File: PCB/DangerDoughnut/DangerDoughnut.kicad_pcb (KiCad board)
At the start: 4 copper layers, 50 x 37 mm, 113 parts, among them J1 Conn_01x02_Pin, J2 Conn_01x02_Pin, J3 Conn_01x02_Pin, J4 Conn_01x04_Pin, J6 USB_C_Receptacle_USB2.0_16P, SW1 SW_Push, SW2 SW_Push, U1 MMC5983MA, U10 ESP32-S3, U2 H3LIS331DLTR, U3 H3LIS331DLTR, U4 W25X20CLZP, U6 L5973D, U7 MIC5219-3.3YM5, U8 ESP8285H16, U9 SX1280IMLTRT, Y1 40MHz, Y2 52MHz, Y3 26MHz

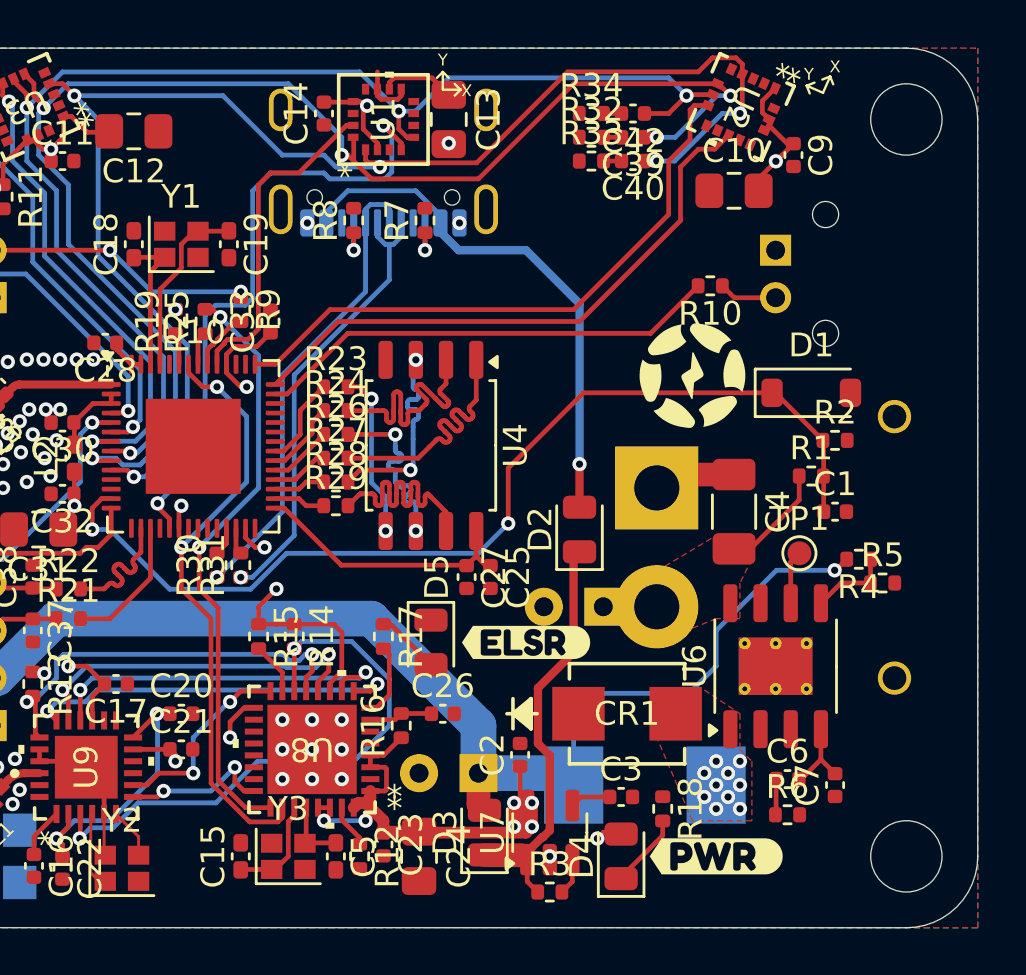
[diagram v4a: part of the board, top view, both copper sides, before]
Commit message: Added silkscreen
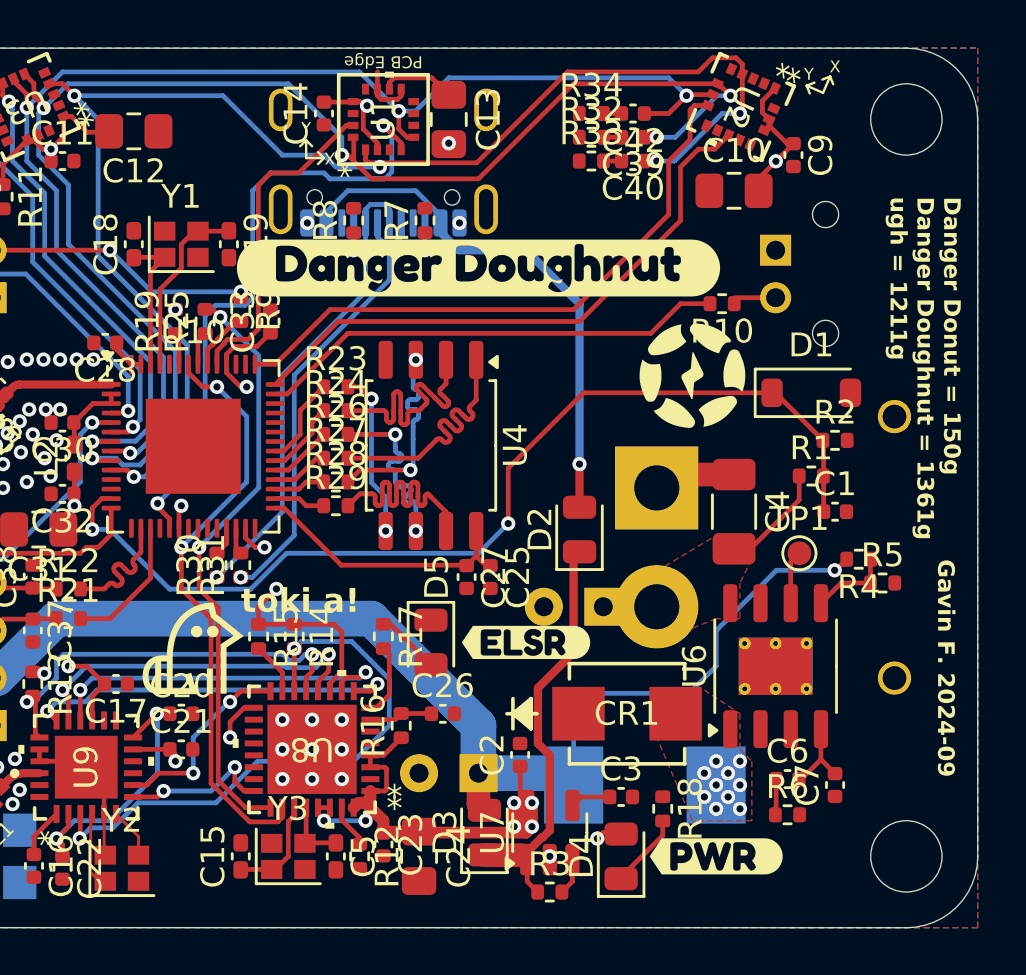
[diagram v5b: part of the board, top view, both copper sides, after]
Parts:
- added kibuzzard-66F236AA: G***, kibuzzard-66F236AA, F.Cu at (104.0, 45.2)
- moved R10 0.90 mm to (114.2, 46.8)
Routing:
- net Net-(J2-Pin_2): track 2.45 -> 1.74 mm
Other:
- board text added: "<--"
- board text added: "<-- Radio waves go here"
- board text added: "Cook Time: 10 minutes Total Time: 2 hours, 30 minutes Yield: 12 donuts and 12 holes Ingredients 1 cup whole milk, warmed to about 110°F 2 and 1/4 teaspoons instant or active dry yeast 1/3 cup granulated sugar, divided 2 large eggs 6 Tablespoons unsalted butter 1/2 teaspoon salt 4 cups all-purpose flour 2 cups confectioners' sugar 1/3 cup heavy cream 1/2 teaspoon pure vanilla extract 1. Prepare th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"
- board text added: "Danger Donut = 150g Danger Doughnut = 1361g ugh = 1211g"
- board text added: "Ferrous metal under the compass! Surely this won't be a problem"
- board text added: "Gavin F. 2024-09"
- board text added: "TODO: layout test points/headers run traces silk screen flip LED wiring move ESC resistors"
- board text added: "toki a!"
- board text removed: "TODO: layout sensors layout esp32 layout test points/headers run traces silk screen flip LED wiring"

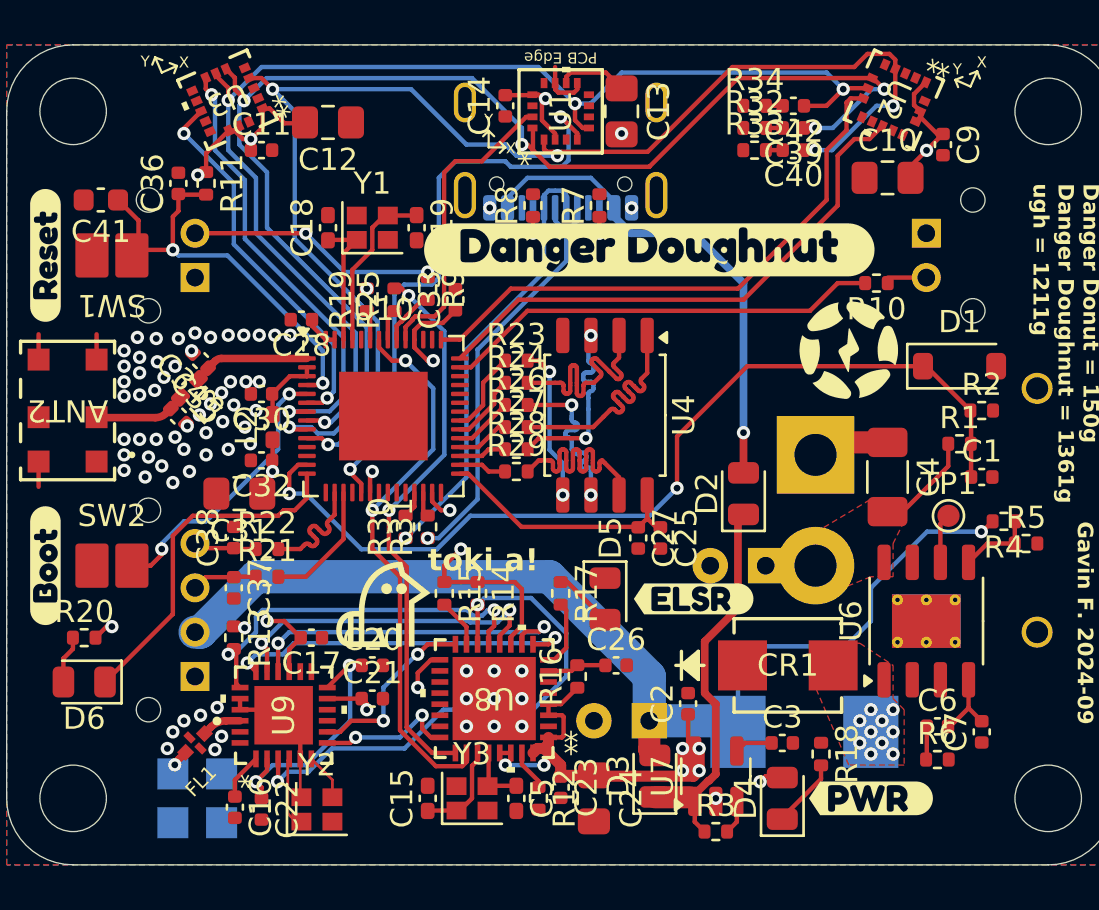
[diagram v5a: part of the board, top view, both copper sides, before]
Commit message: main layout complete needs headers and testpoints
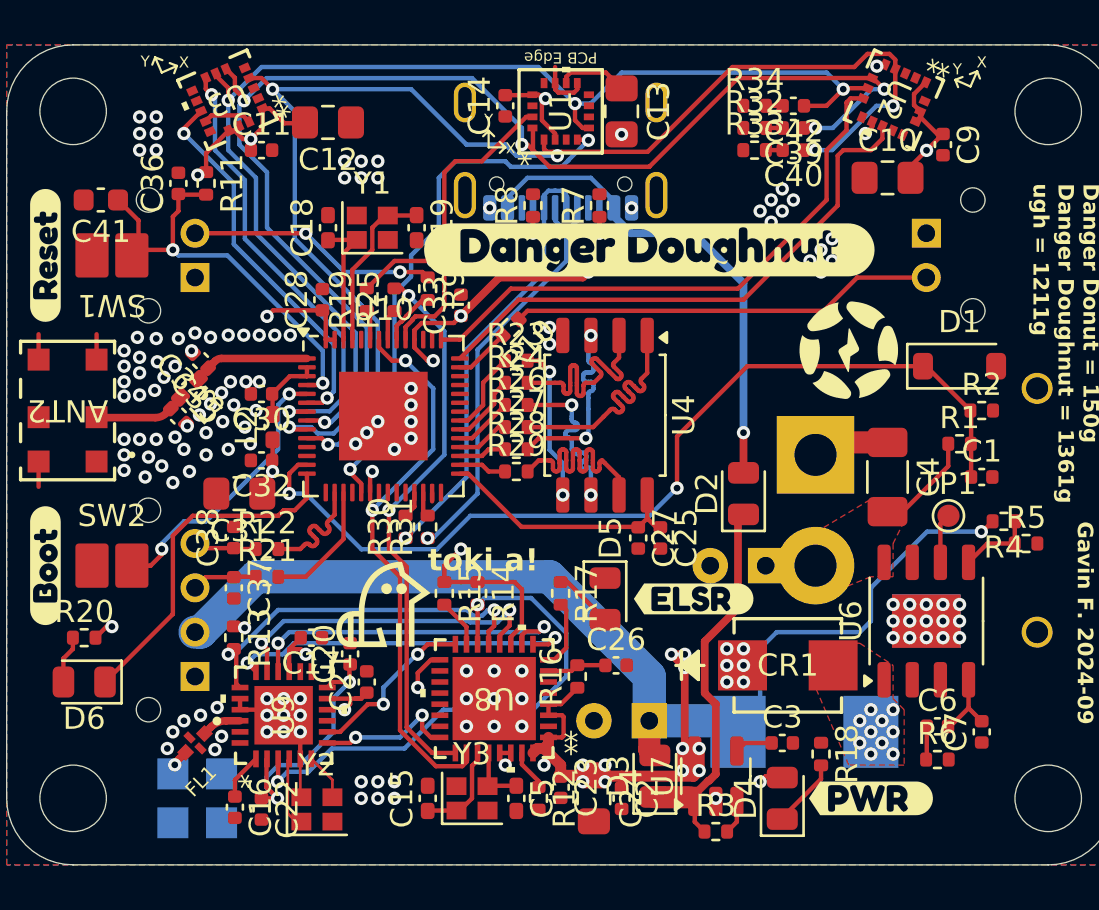
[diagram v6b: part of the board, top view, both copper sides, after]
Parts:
- moved R10 16.6 mm to (97.8, 48.8), turned to -135 degrees
- moved C2 5.22 mm to (102.8, 70.0), turned to -90 degrees
- moved C28 1.31 mm to (89.2, 47.5), turned to 90 degrees
- moved C20 1.13 mm to (90.5, 63.5), turned to 90 degrees
- moved C21 0.79 mm to (91.2, 64.8), turned to 90 degrees
- moved C33 0.35 mm to (95.5, 47.8)
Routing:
- net +3.3V: track 70.3 -> 88.5 mm, vias 20 -> 30
- net Net-(J2-Pin_2): track 1.74 -> 19.2 mm
- net ESC_R: track 19.9 -> 2.54 mm
- net GND: track 16.4 -> 20.4 mm, vias 70 -> 142
- net Mag_CS: track 26.6 -> 24.2 mm
- net unconnected-(U10-GPIO21-Pad27): track 1.37 -> 0.40 mm, vias 1 -> 0
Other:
- board text added: "TODO: layout test points/headers"
- board text removed: "TODO: layout test points/headers run traces silk screen flip LED wiring move ESC resistors"

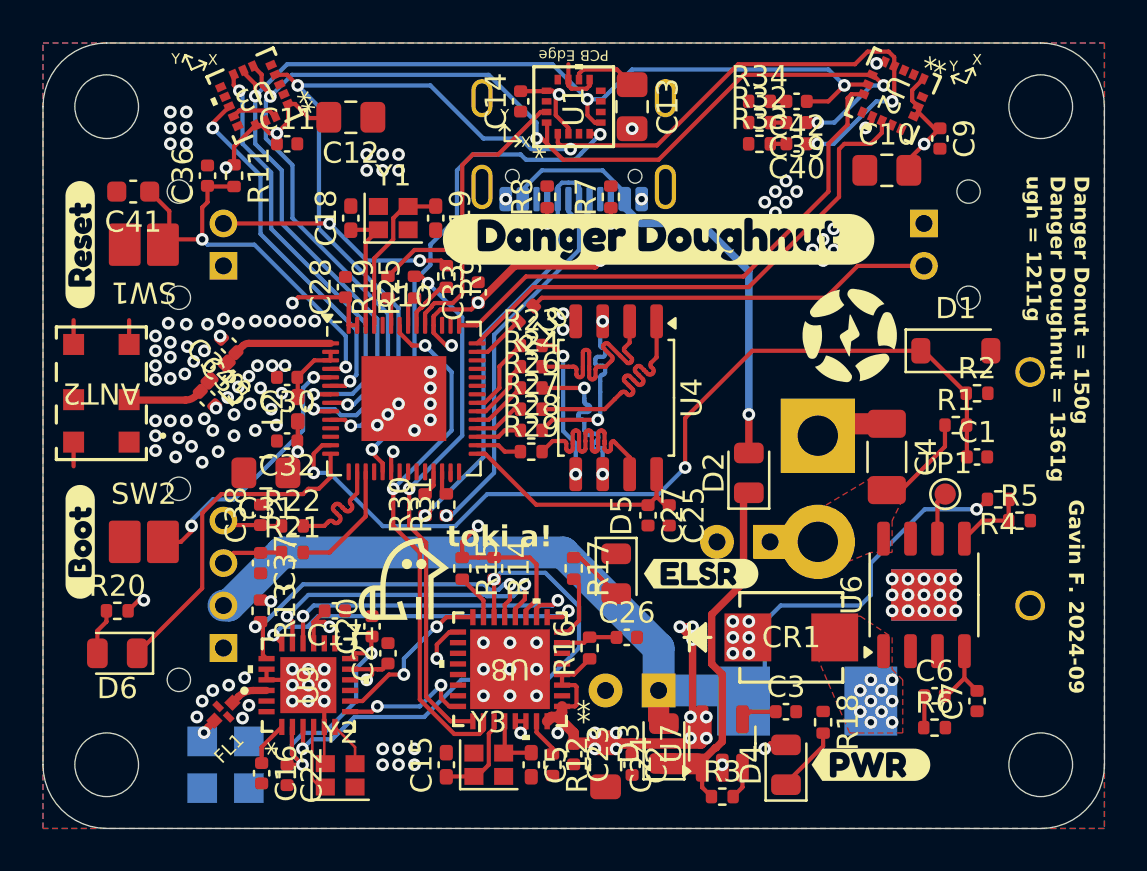
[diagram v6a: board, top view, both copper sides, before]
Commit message: esp32 pins checked
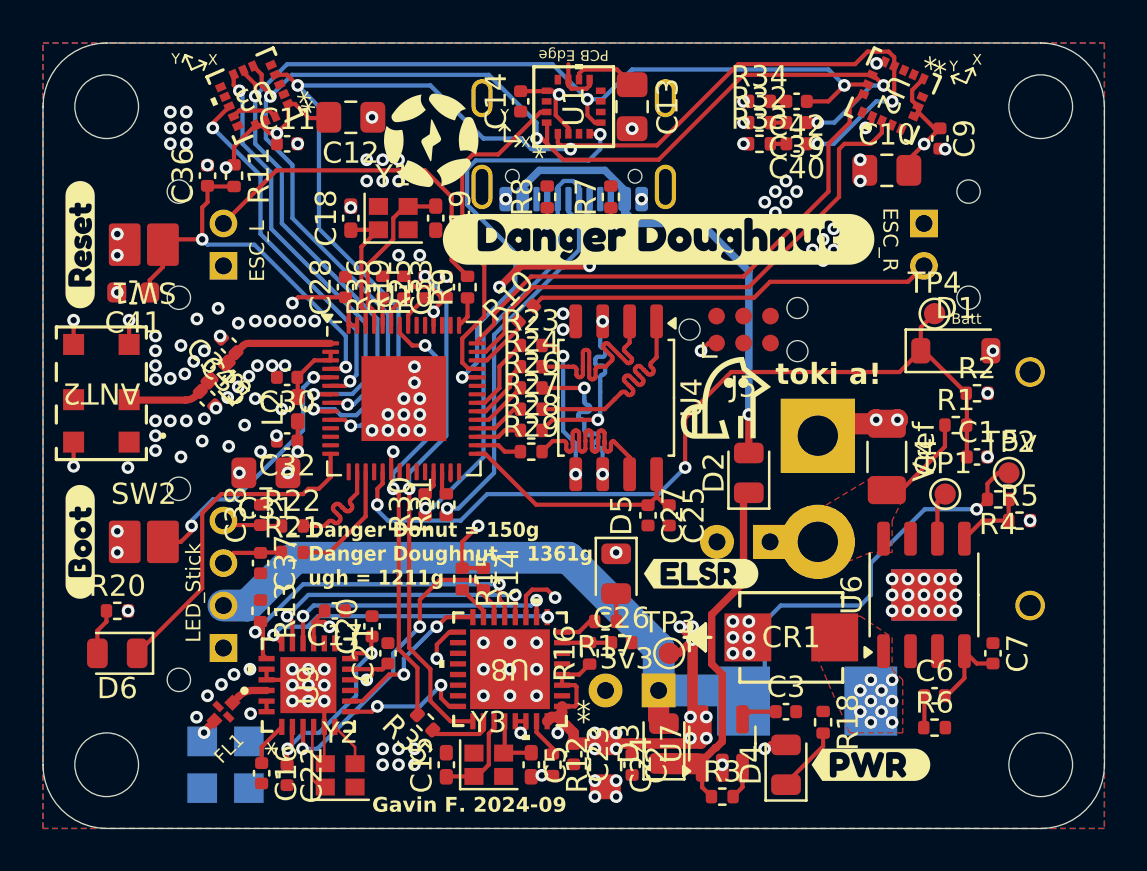
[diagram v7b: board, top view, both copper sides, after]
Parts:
- added J5: TC2030-NL, Connector:Tag-Connect_TC2030-IDC-NL_2x03_P1.27mm_Vertical, F.Cu at (108.0, 49.5)
- added R35: 510, Resistor_SMD:R_0402_1005Metric, F.Cu at (93.0, 68.0)
- added R36: 10K, Resistor_SMD:R_0402_1005Metric, F.Cu at (91.0, 47.5)
- added TP2: 5v, TestPoint:TestPoint_Pad_D1.0mm, F.Cu at (120.5, 56.2)
- added TP3: 3v3, TestPoint:TestPoint_Pad_D1.0mm, F.Cu at (104.5, 64.8)
- added TP4: Batt, TestPoint:TestPoint_Pad_D1.0mm, F.Cu at (117.0, 48.8)
- R10, R9: value 100 -> 33
- moved C41 4.75 mm to (79.2, 47.8)
- moved R17 2.92 mm to (101.5, 63.2), turned to 180 degrees
- moved C7 2.37 mm to (119.8, 64.8), turned to -90 degrees
- moved C33 1.52 mm to (94.0, 47.5)
- moved R9 1.12 mm to (95.0, 47.5), turned to 90 degrees
- moved R19 0.75 mm to (92.0, 47.5)
- moved R14 0.71 mm to (95.8, 61.2)
- moved R15 0.50 mm to (94.8, 61.2)
- moved R25 0.50 mm to (93.0, 47.5)
- moved C26 0.35 mm to (102.2, 64.2)
- moved R16 0.25 mm to (100.8, 64.8)
- turned R10 to 45 degrees
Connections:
- J2 pad 2: Net-(J2-Pin_2) -> ESC_R
- J3 pad 2: Net-(J3-Pin_2) -> ESC_L
- R10 pad 1: Net-(J2-Pin_2) -> Net-(U10-GPIO35)
- R9 pad 1: Net-(J3-Pin_2) -> Net-(U10-GPIO38)
- U10 pad 13: BATT -> unconnected-(U10-GPIO8-Pad13)
- U10 pad 19: Mag_CS -> BATT
- U10 pad 38: unconnected-(U10-GPIO33-Pad38) -> Mag_CS
- U10 pad 39: unconnected-(U10-GPIO34-Pad39) -> MAG_INT
- U10 pad 40: unconnected-(U10-GPIO35-Pad40) -> Net-(U10-GPIO35)
- U10 pad 41: ESC_R -> ACCEL1_INT
- U10 pad 42: ACCEL1_INT -> Accel1_CS
- U10 pad 43: Accel1_CS -> Net-(U10-GPIO38)
- U10 pad 47: MAG_INT -> unconnected-(U10-MTDI-Pad47)
- U10 pad 48: ESC_L -> unconnected-(U10-MTMS-Pad48)
- U10 pad 52: unconnected-(U10-GPIO46-Pad52) -> Net-(U10-GPIO46)
- U8 pad 26: ELSR_TX -> Net-(U8-U0TXD)
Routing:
- net Net-(J2-Pin_2): track 19.2 -> 0.00 mm
- net ESC_R: track 2.54 -> 19.2 mm
- net ESC_L: track 2.53 -> 16.4 mm
- net Net-(J3-Pin_2): track 11.3 -> 0.00 mm, vias 2 -> 0
- net N_RST: track 24.6 -> 15.6 mm
- net +3.3V: track 88.5 -> 82.3 mm, vias 30 -> 32
- net ELSR_TX: track 24.8 -> 20.7 mm
- net Mag_CS: track 24.2 -> 20.4 mm
- net Net-(U8-U0TXD): track 0.00 -> 2.96 mm
- net Net-(U10-GPIO35): track 0.00 -> 2.91 mm
- net MAG_INT: track 13.8 -> 16.0 mm
- net SX_SCK: track 16.1 -> 13.9 mm
- net GND: track 20.4 -> 22.4 mm, vias 142 -> 168
- net BATT: track 42.3 -> 40.4 mm
- net /DCC_FB: track 12.2 -> 10.4 mm
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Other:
- board text added: "ESC_L"
- board text added: "ESC_R"
- board text added: "LED_Stick"

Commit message: test points done
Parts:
- removed J5: TC2030-NL, Connector:Tag-Connect_TC2030-IDC-NL_2x03_P1.27mm_Vertical
- added J10: Conn_01x01_Pin, Connector_Wire:SolderWirePad_1x01_SMD_1x2mm, F.Cu at (123.2, 53.2)
- added J11: Conn_01x01_Pin, Connector_Wire:SolderWirePad_1x01_SMD_1x2mm, F.Cu at (123.2, 60.8)
- added J12: Conn_01x01_Pin, Connector_Wire:SolderWirePad_1x01_SMD_1x2mm, F.Cu at (123.2, 65.8)
- added J13: Conn_01x01_Pin, Connector_Wire:SolderWirePad_1x01_SMD_1x2mm, F.Cu at (123.2, 45.2)
- added J14: Conn_01x01_Pin, Connector_Wire:SolderWirePad_1x01_SMD_1x2mm, F.Cu at (123.2, 57.8)
- added J15: Conn_01x01_Pin, Connector_Wire:SolderWirePad_1x01_SMD_1x2mm, F.Cu at (123.2, 49.8)
- added J16: Conn_01x01_Pin, Connector_Wire:SolderWirePad_1x01_SMD_1x2mm, F.Cu at (123.2, 43.8)
- added J17: Conn_01x01_Pin, Connector_Wire:SolderWirePad_1x01_SMD_1x2mm, F.Cu at (123.2, 48.2)
- added J19: Conn_01x01_Pin, Connector_Wire:SolderWirePad_1x01_SMD_1x2mm, F.Cu at (123.2, 46.8)
- added J20: Conn_01x01_Pin, Connector_Wire:SolderWirePad_1x01_SMD_1x2mm, F.Cu at (123.2, 64.2)
- added J7: Conn_01x01_Pin, Connector_Wire:SolderWirePad_1x01_SMD_1x2mm, F.Cu at (123.2, 56.2)
- added J8: Conn_01x01_Pin, Connector_Wire:SolderWirePad_1x01_SMD_1x2mm, F.Cu at (123.2, 54.8)
- added J9: Conn_01x01_Pin, Connector_Wire:SolderWirePad_1x01_SMD_1x2mm, F.Cu at (123.2, 59.2)
- added JP1: SolderJumper_2_Open, Jumper:SolderJumper-2_P1.3mm_Open_RoundedPad1.0x1.5mm, F.Cu at (92.5, 70.0)
- added TP10: A1_CS, Danger_Doughnut_Lib:Test_Via, F.Cu at (111.0, 42.0)
- added TP11: A1_INT, Danger_Doughnut_Lib:Test_Via, F.Cu at (113.2, 43.5)
- added TP12: A2_CS, Danger_Doughnut_Lib:Test_Via, F.Cu at (82.0, 38.0)
- added TP13: A2_INT, Danger_Doughnut_Lib:Test_Via, F.Cu at (82.8, 40.0)
- added TP14: MAG_CS, Danger_Doughnut_Lib:Test_Via, F.Cu at (94.0, 41.8)
- added TP15: MAG_INT, Danger_Doughnut_Lib:Test_Via, F.Cu at (94.0, 40.0)
- added TP16: BATT, Danger_Doughnut_Lib:Test_Via, F.Cu at (114.2, 50.0)
- added TP17: SX_MOSI, Danger_Doughnut_Lib:Test_Via_small, F.Cu at (86.5, 63.0)
- added TP18: LED_MOSI, Danger_Doughnut_Lib:Test_Via, F.Cu at (82.8, 56.8)
- added TP19: LED_SCK, Danger_Doughnut_Lib:Test_Via, F.Cu at (81.8, 62.0)
- added TP20: ESC_L, Danger_Doughnut_Lib:Test_Via, F.Cu at (89.0, 41.2)
- added TP21: ESC_R, Danger_Doughnut_Lib:Test_Via, F.Cu at (111.0, 48.5)
- added TP22: SX_SCK, Danger_Doughnut_Lib:Test_Via_small, F.Cu at (86.0, 63.8)
- added TP23: SX_CS, Danger_Doughnut_Lib:Test_Via_small, F.Cu at (85.0, 63.8)
- added TP24: Busy, Danger_Doughnut_Lib:Test_Via_small, F.Cu at (93.8, 66.2)
- added TP25: RST, Danger_Doughnut_Lib:Test_Via_small, F.Cu at (92.8, 64.0)
- added TP26: 5v, Danger_Doughnut_Lib:Test_Via, F.Cu at (120.5, 60.0)
- added TP27: 3v3, Danger_Doughnut_Lib:Test_Via, F.Cu at (105.2, 62.8)
- added TP28: GND, Danger_Doughnut_Lib:Test_Via, F.Cu at (105.2, 71.5)
- added TP5: MISO, Danger_Doughnut_Lib:Test_Via, F.Cu at (112.2, 38.2)
- added TP6: MOSI, Danger_Doughnut_Lib:Test_Via, F.Cu at (106.2, 41.0)
- added TP7: SCK, Danger_Doughnut_Lib:Test_Via, F.Cu at (106.0, 38.2)
- added TP8: ELSR_TX, Danger_Doughnut_Lib:Test_Via, F.Cu at (92.0, 68.0)
- added TP9: ELSR_RX, Danger_Doughnut_Lib:Test_Via, F.Cu at (93.0, 46.2)
- TP4: value Batt -> SX_MISO; footprint TestPoint:TestPoint_Pad_D1.0mm -> Danger_Doughnut_Lib:Test_Via_small
- moved TP4 33.0 mm to (87.2, 63.0)
- moved R31 0.56 mm to (94.5, 57.5), turned to 180 degrees
- moved C20 0.34 mm to (90.2, 63.2)
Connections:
- TP4 pad 1: BATT -> SX_MISO
- U10 pad 11: unconnected-(U10-GPIO6-Pad11) -> Net-(J7-Pin_1)
- U10 pad 12: unconnected-(U10-GPIO7-Pad12) -> Net-(J8-Pin_1)
- U10 pad 13: unconnected-(U10-GPIO8-Pad13) -> Net-(J9-Pin_1)
- U10 pad 23: unconnected-(U10-GPIO17-Pad23) -> Net-(J10-Pin_1)
- U10 pad 24: unconnected-(U10-GPIO18-Pad24) -> Net-(J11-Pin_1)
- U10 pad 44: unconnected-(U10-MTCK-Pad44) -> Net-(J13-Pin_1)
- U10 pad 48: unconnected-(U10-MTMS-Pad48) -> Net-(J16-Pin_1)
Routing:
- net Net-(J9-Pin_1): track 0.00 -> 42.0 mm, vias 0 -> 4
- net Net-(J7-Pin_1): track 0.00 -> 40.9 mm, vias 0 -> 4
- net Net-(J8-Pin_1): track 0.00 -> 39.1 mm, vias 0 -> 4
- net Net-(J16-Pin_1): track 0.00 -> 36.2 mm, vias 0 -> 6
- net Net-(J11-Pin_1): track 0.00 -> 34.3 mm, vias 0 -> 4
- net Net-(J10-Pin_1): track 0.00 -> 34.2 mm, vias 0 -> 4
- net Net-(J13-Pin_1): track 0.00 -> 34.0 mm, vias 0 -> 6
- net GPIO0: track 1.71 -> 10.8 mm, vias 0 -> 2
- net +5V: track 50.9 -> 56.0 mm, vias 1 -> 4
- net +3.3V: track 82.3 -> 87.1 mm, vias 32 -> 36
- net Net-(J4-Pin_3): track 2.95 -> 5.32 mm
- net Accel2_CS: track 20.5 -> 22.7 mm
- net Net-(J4-Pin_4): track 2.84 -> 4.90 mm
- net Net-(U10-GPIO0): track 12.6 -> 14.3 mm
- net MAG_INT: track 16.0 -> 17.7 mm
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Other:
- board text removed: "ESC_L"
- board text removed: "ESC_R"
- board text removed: "LED_Stick"
- board text removed: "TODO: layout test points/headers"
